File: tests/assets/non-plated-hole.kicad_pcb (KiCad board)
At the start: 2 copper layers, 50 x 50 mm, 2 parts

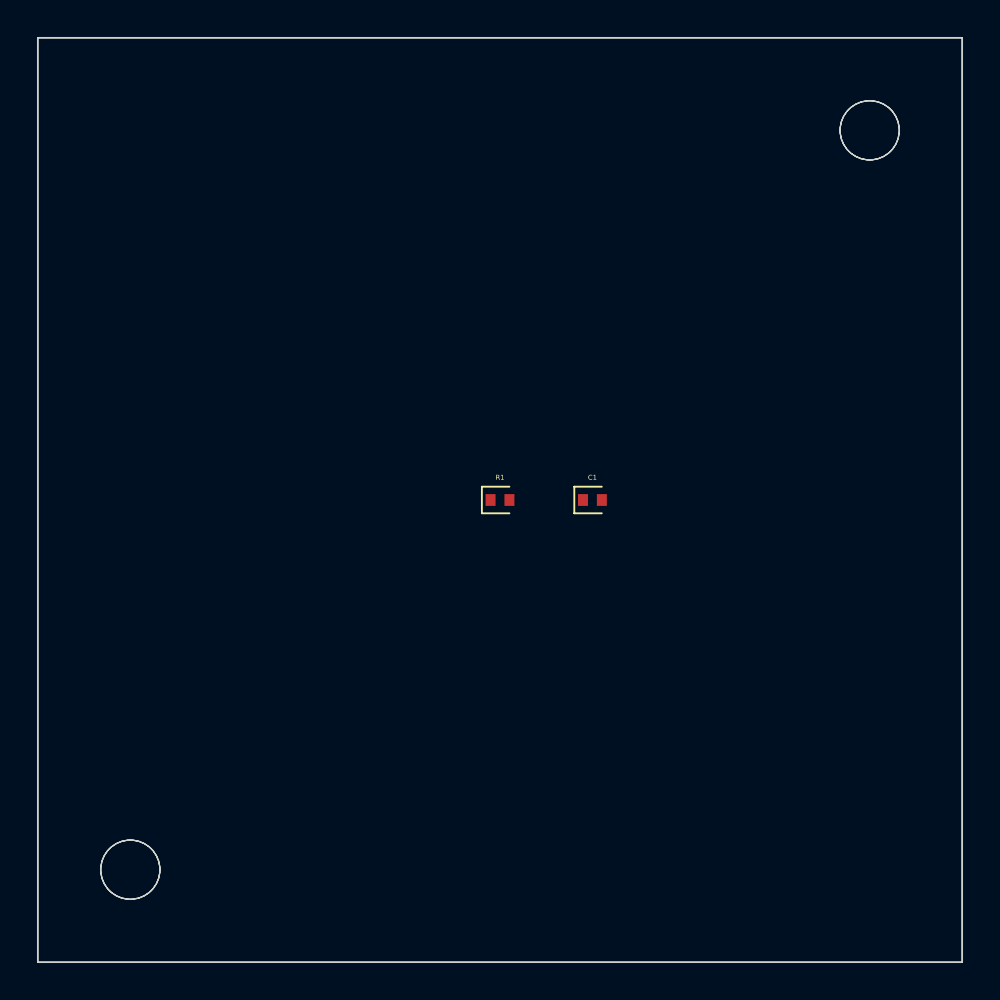
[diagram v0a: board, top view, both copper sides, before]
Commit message: feat: Implement a dedicated stage for standalone pcb elements and correct hole association in component footprints (#170)
* feat: Implement a dedicated stage for standalone non-plated holes and correct hole association in component footprints

* up

* update

* update

* up

* up

* up

* up

* up
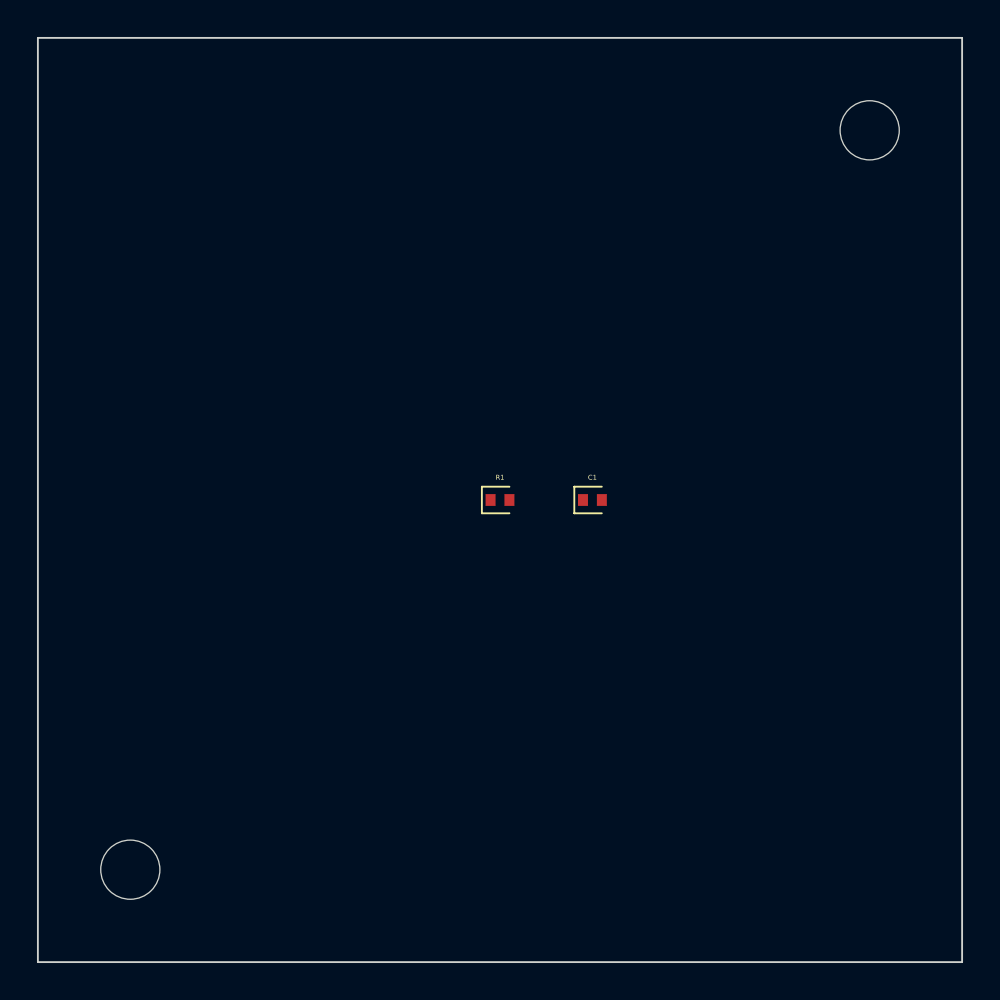
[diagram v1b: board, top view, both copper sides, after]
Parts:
- added ? (x2): , tscircuit:MountingHole, F.Cu at (100.0, 100.0)
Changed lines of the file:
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@@
       (layers F.Cu F.Paste F.Mask)
-    )
-    (pad "" np_thru_hole circle
-      (at -20 20 0)
-      (size 3.2 3.2)
-      (drill 3.2)
-      (layers *.Cu *.Mask)
-    )
-    (pad "" np_thru_hole circle
-      (at 20 -20 0)
-      (size 3.2 3.2)
-      (drill 3.2)
-      (layers *.Cu *.Mask)
     )
   )
@@
       (layers F.Cu F.Paste F.Mask)
     )
+  )
+  (footprint
+    "tscircuit:MountingHole"
+    (layer F.Cu)
+    (at 100 100 0)
     (pad "" np_thru_hole circle
-      (at -25 20 0)
+      (at -20 20 0)
       (size 3.2 3.2)
       (drill 3.2)
       (layers *.Cu *.Mask)
     )
+  )
+  (footprint
+    "tscircuit:MountingHole"
+    (layer F.Cu)
+    (at 100 100 0)
     (pad "" np_thru_hole circle
-      (at 15 -20 0)
+      (at 20 -20 0)
       (size 3.2 3.2)
       (drill 3.2)

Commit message: feat: Dynamically footprints name for standalone PCB hole footprints in KiCad based on their shape and dimensions (#179)
* feat: Dynamically name standalone PCB hole footprints in KiCad based on their shape and dimensions

* update

* ne

* up

* up

* up test

* f
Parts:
- ? (x2): footprint tscircuit:MountingHole -> tscircuit:hole_circle_holeDiameter3.2mm
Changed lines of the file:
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@@
   )
   (footprint
-    "tscircuit:MountingHole"
+    "tscircuit:hole_circle_holeDiameter3.2mm"
     (layer F.Cu)
     (at 100 100 0)
@@
   )
   (footprint
-    "tscircuit:MountingHole"
+    "tscircuit:hole_circle_holeDiameter3.2mm"
     (layer F.Cu)
     (at 100 100 0)
